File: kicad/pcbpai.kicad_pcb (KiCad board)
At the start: 2 copper layers, 91.4 x 109.2 mm, 19 parts, among them J1 Fusible, J2 Conn_01x04_Pin, J3 Input 24 V, J4 Boton Encendido, J5 Parada de Emergencia, J6 Conn_01x06_Pin, J8 Conn_01x09_Pin, M1 MountingHole_2.5mm_Pad, SW1 SW_Push_DPDT, U6 ATtiny85-20P

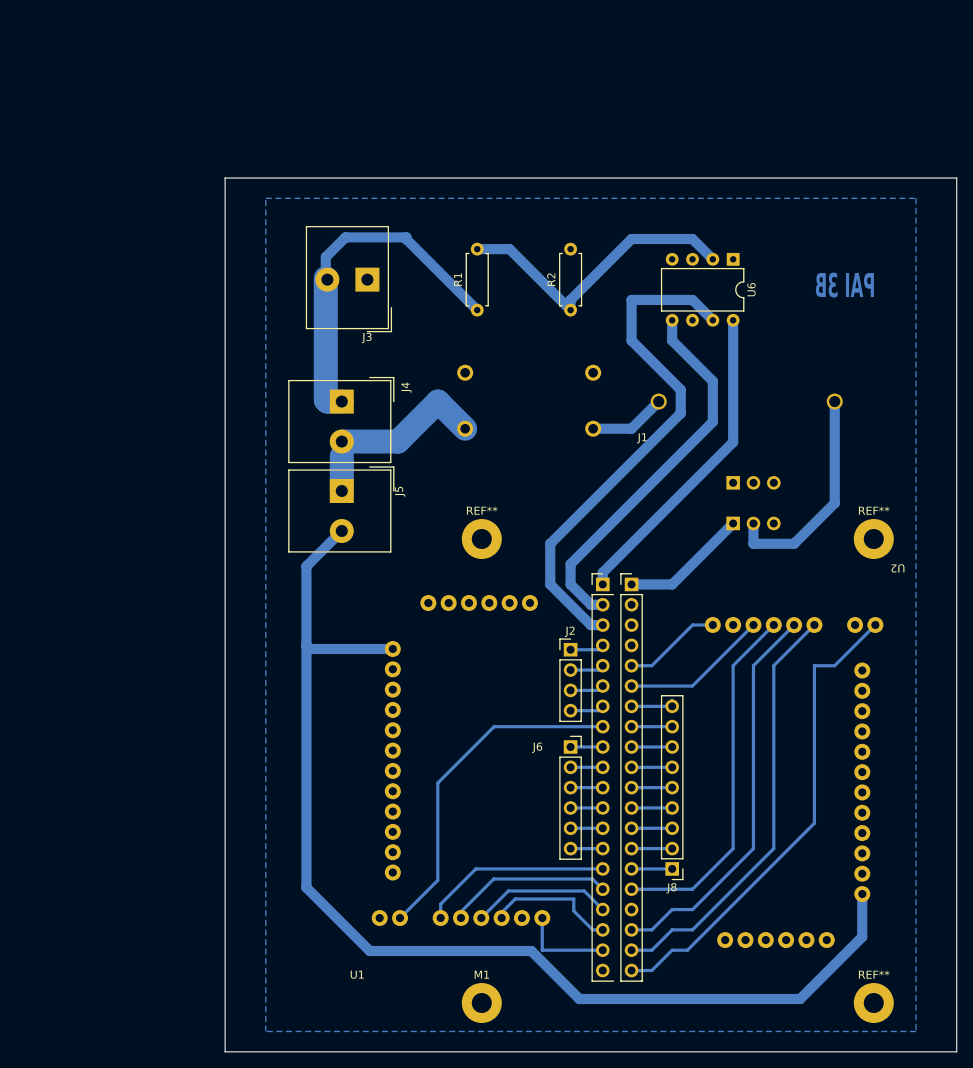
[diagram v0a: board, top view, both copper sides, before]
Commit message: add 3d models and footprints to kicad
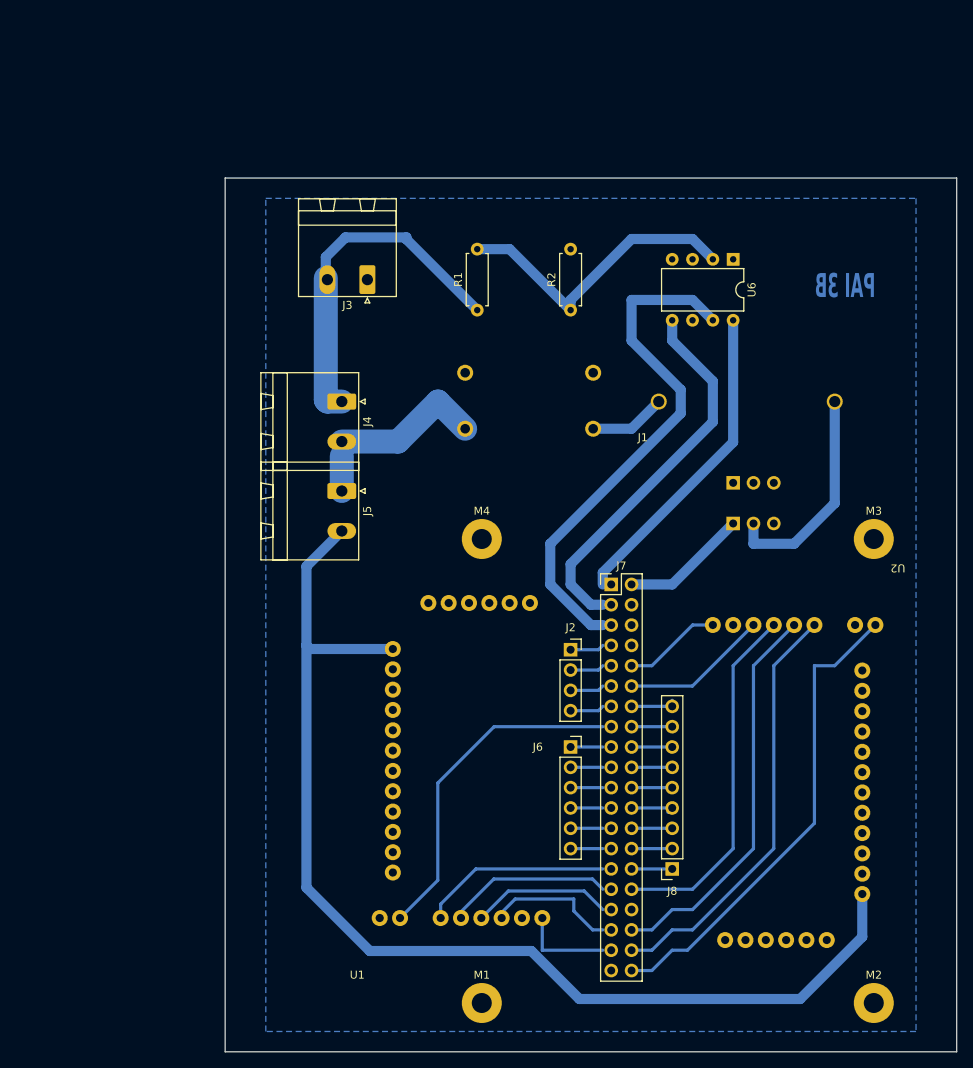
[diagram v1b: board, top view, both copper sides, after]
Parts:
- removed U3: ~, libpai:raspberry
- added J7: Raspberry GPIO, Connector_PinHeader_2.54mm:PinHeader_2x20_P2.54mm_Vertical, F.Cu at (170.2, 106.7)
- J2: footprint Connector_PinHeader_2.54mm:PinHeader_1x04_P2.54mm_Vertical -> Connector_PinSocket_2.54mm:PinSocket_1x04_P2.54mm_Vertical
- J3, J4, J5: footprint TerminalBlock_Altech:Altech_AK300_1x02_P5.00mm_45-Degree -> Connector_Phoenix_MSTB:PhoenixContact_MSTBA_2,5_2-G_1x02_P5.00mm_Horizontal
- J8: footprint Connector_PinHeader_2.54mm:PinHeader_1x09_P2.54mm_Vertical -> Connector_PinSocket_2.54mm:PinSocket_1x09_P2.54mm_Vertical
- SW1: footprint libpai:pulsador -> PAI:pulsador
- U1, U2: footprint libpai:Pololu MAX 14870 Dual Shield Arduino -> PAI:Pololu MAX 14870 Dual Shield Arduino
- renumbered REF** to M2, REF** to M3, REF** to M4

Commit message: center raspberry mounting holes
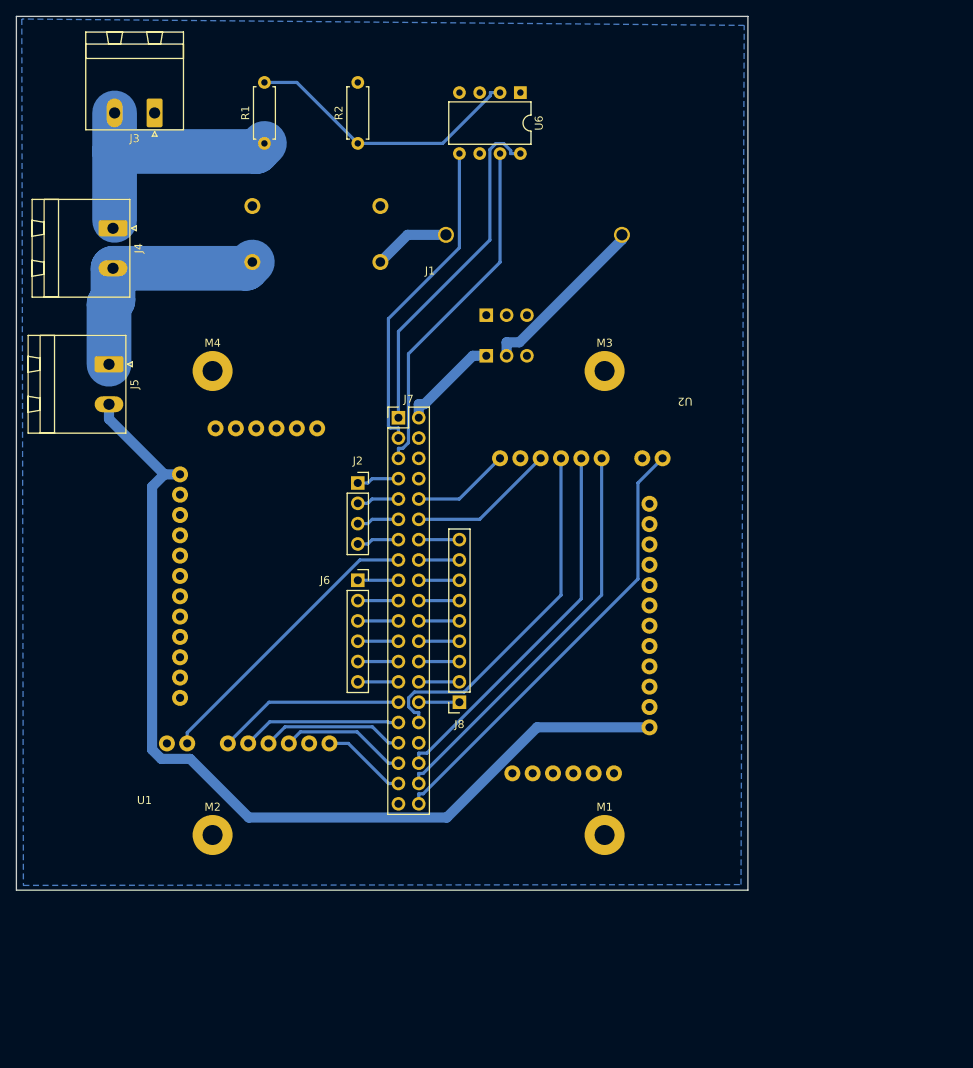
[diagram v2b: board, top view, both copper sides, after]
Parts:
- moved M2 85.3 mm to (120.3, 138.0)
- moved M3 39.7 mm to (169.3, 80.0)
- moved M4 39.7 mm to (120.3, 80.0)
- moved SW1 37.3 mm to (153.5, 76.9)
- moved J4 35.9 mm to (107.9, 62.2)
- moved U1 34.4 mm to (111.8, 134.2)
- moved J8 33.8 mm to (151.2, 121.4)
- moved U4 33.8 mm to (142.3, 67.4)
- moved R1 33.8 mm to (126.8, 51.5)
- moved J2 33.8 mm to (138.5, 94.0)
- moved J6 33.8 mm to (138.5, 106.2)
- moved J7 33.8 mm to (143.6, 85.8)
- moved R2 33.8 mm to (138.5, 51.5)
- moved U2 33.8 mm to (179.4, 83.3)
- moved U6 33.8 mm to (158.8, 45.2)
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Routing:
- net Net-(J5-Pin_2): track 141.2 -> 119.0 mm
- net Net-(J7-Pin_5): track 64.7 -> 43.7 mm
- net +24V: track 43.5 -> 33.7 mm
- net Net-(J7-Pin_3): track 47.6 -> 40.3 mm
- net Net-(J4-Pin_2): track 23.3 -> 30.0 mm
- net Net-(J7-Pin_15): track 42.4 -> 36.7 mm
- net Net-(J1-Pin_2): track 27.6 -> 22.0 mm
- net Net-(J7-Pin_40): track 59.9 -> 56.1 mm
- net Net-(J7-Pin_1): track 39.8 -> 43.1 mm
- net Net-(J7-Pin_2): track 15.9 -> 12.6 mm
- net Net-(J7-Pin_38): track 53.1 -> 50.4 mm
- net Net-(U6-XTAL1/PB3): track 38.1 -> 35.5 mm
- net Net-(J7-Pin_36): track 49.5 -> 47.1 mm
- net Net-(J2-Pin_4): track 4.24 -> 5.30 mm
- net Net-(J2-Pin_2): track 4.24 -> 5.30 mm
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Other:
- board text removed: "PAI 3B"

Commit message: update libraries and change trace width
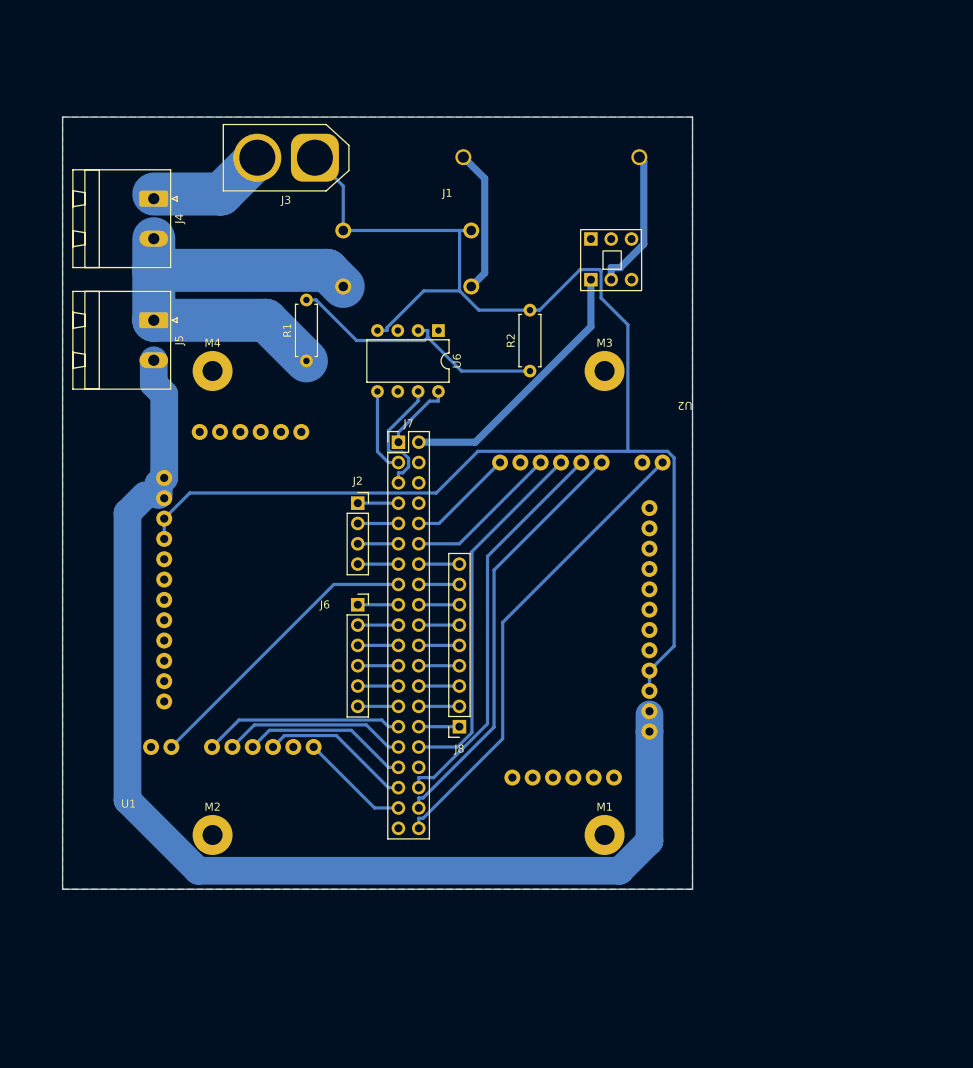
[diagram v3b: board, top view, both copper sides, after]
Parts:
- J1: footprint libpai:fusible -> PAI:fusible
- J3: footprint Connector_Phoenix_MSTB:PhoenixContact_MSTBA_2,5_2-G_1x02_P5.00mm_Horizontal -> Connector_AMASS:AMASS_XT60-M_1x02_P7.20mm_Vertical
- SW1: footprint PAI:pulsador -> PAI:switch
- U4: footprint libpai:regulador -> PAI:regulador
- moved R2 35.7 mm to (160.0, 80.0)
- moved U6 31.5 mm to (148.6, 74.9)
- moved R1 27.7 mm to (132.1, 78.7)
- moved J3 20.8 mm to (133.1, 53.3)
- moved SW1 16.2 mm to (166.6, 67.4)
- moved U4 11.8 mm to (153.7, 70.4)
- moved J1 9.95 mm to (149.7, 58.3)
- moved J5 7.85 mm to (113.0, 73.7)
- moved J4 6.30 mm to (113.0, 58.5)
- moved J6 3.06 mm to (138.5, 109.2)
- moved J7 3.06 mm to (143.6, 88.9)
- moved J8 3.06 mm to (151.2, 124.5)
- moved J2 2.52 mm to (138.5, 96.5)
- moved U1 2.03 mm to (109.8, 134.6)
- moved U2 0.53 mm to (179.4, 83.8)
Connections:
- R1 pad 1: +24V -> Net-(J4-Pin_2)
- U1 pad 10: unconnected-(U1-GND_2-Pad10) -> GND
- U1 pad 8: unconnected-(U1-Vin_2-Pad8) -> Net-(J5-Pin_2)
- U2 pad 10: unconnected-(U2-GND_2-Pad10) -> GND
- U2 pad 8: unconnected-(U2-Vin_2-Pad8) -> Net-(J5-Pin_2)
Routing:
- net GND: track 0.00 -> 191.9 mm
- net Net-(J7-Pin_1): track 43.1 -> 9.06 mm
- net Net-(J7-Pin_3): track 40.3 -> 10.7 mm
- net Net-(J7-Pin_5): track 43.7 -> 15.7 mm
- net Net-(J5-Pin_2): track 119.0 -> 146.8 mm
- net Net-(J4-Pin_2): track 30.0 -> 55.9 mm
- net Net-(J7-Pin_2): track 12.6 -> 33.4 mm
- net +24V: track 33.7 -> 14.8 mm
- net Net-(J1-Pin_1): track 9.60 -> 18.0 mm
- net Net-(J1-Pin_2): track 22.0 -> 17.9 mm
- net Net-(J7-Pin_31): track 19.9 -> 23.0 mm
- net Net-(J7-Pin_33): track 17.9 -> 21.0 mm
- net Net-(J7-Pin_37): track 10.7 -> 13.8 mm
- net Net-(J7-Pin_35): track 15.9 -> 19.0 mm
- net Net-(J7-Pin_36): track 47.1 -> 50.1 mm
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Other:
- board size 91.4 x 109.2 mm -> 78.7 x 96.5 mm

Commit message: add termninal blocks for sensors and 24+ zone
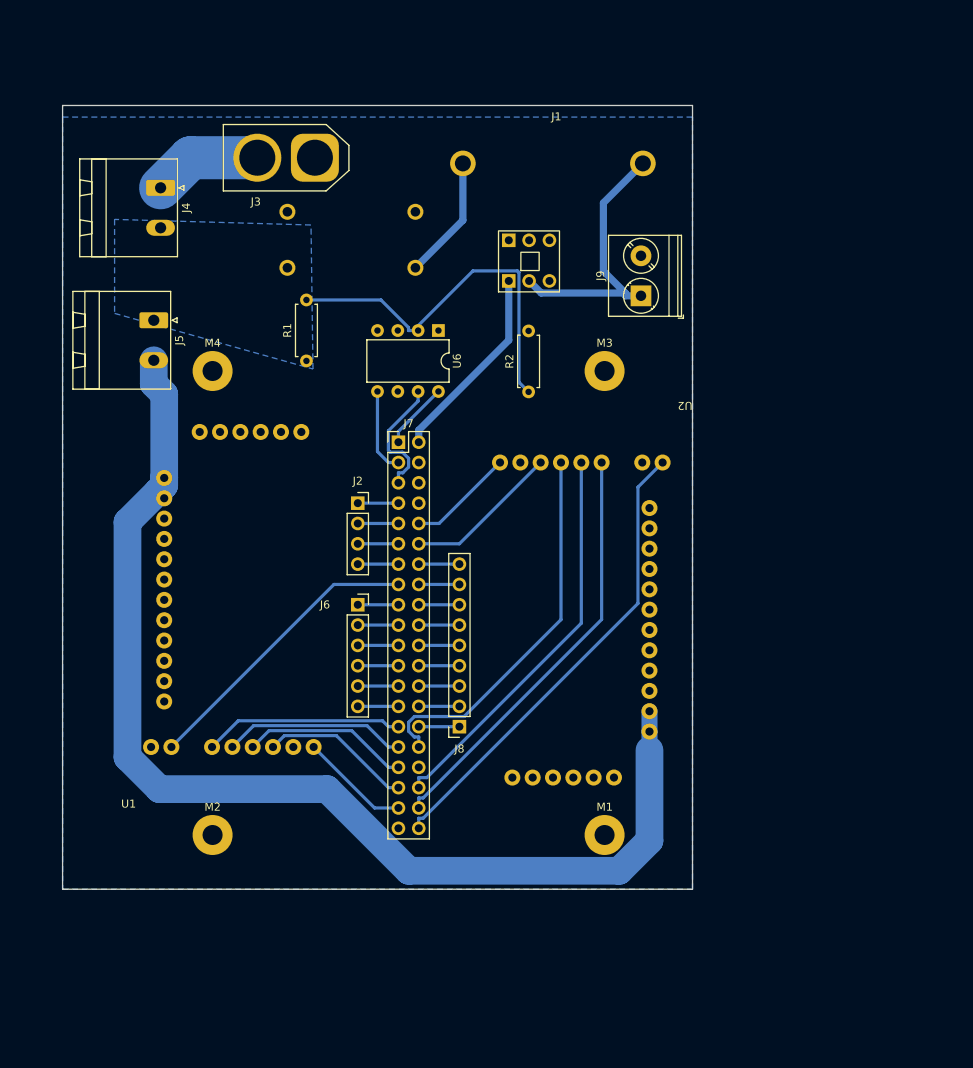
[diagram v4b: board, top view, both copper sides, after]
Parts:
- added J9: Conn_01x02_Socket, TerminalBlock_Phoenix:TerminalBlock_Phoenix_PT-1,5-2-5.0-H_1x02_P5.00mm_Horizontal, F.Cu at (173.9, 70.6)
- J1: value Fusible -> Fuse; footprint PAI:fusible -> PAI:fuse
- moved SW1 10.3 mm to (156.3, 67.6)
- moved U4 7.36 mm to (146.7, 68.1)
- moved J1 4.65 mm to (151.6, 54.0)
- moved R2 2.61 mm to (159.8, 82.6)
- moved J4 1.61 mm to (113.8, 57.1)
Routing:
- net GND: track 191.9 -> 0.00 mm
- net Net-(J4-Pin_2): track 55.9 -> 0.00 mm
- net Net-(J1-Pin_2): track 17.9 -> 34.3 mm
- net Net-(U6-XTAL1/PB3): track 34.0 -> 47.6 mm
- net Net-(J7-Pin_2): track 33.4 -> 24.8 mm
- net Net-(J5-Pin_2): track 146.8 -> 142.1 mm
- net Net-(J1-Pin_1): track 18.0 -> 15.5 mm
- net Net-(J7-Pin_32): track 45.8 -> 47.9 mm
- net +24V: track 14.8 -> 13.6 mm
- net Net-(J7-Pin_1): track 9.06 -> 8.41 mm
- added copper zone on B.Cu, net Net-(J4-Pin_2)
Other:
- board size 78.7 x 96.5 mm -> 78.7 x 98 mm

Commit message: finish pcb
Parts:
- removed SW1: SW_Push_DPDT, PAI:switch
- removed U1, U2: ~, PAI:Pololu MAX 14870 Dual Shield Arduino
- added D1: ~, Connector_PinHeader_2.54mm:PinHeader_2x04_P2.54mm_Vertical, F.Cu at (159.0, 86.9)
- added D2: ~, Connector_PinHeader_2.54mm:PinHeader_2x04_P2.54mm_Vertical, F.Cu at (159.0, 123.0)
- added D3: ~, Connector_PinHeader_2.54mm:PinHeader_2x04_P2.54mm_Vertical, F.Cu at (129.0, 94.8)
- added D4: ~, Connector_PinHeader_2.54mm:PinHeader_2x04_P2.54mm_Vertical, F.Cu at (129.0, 130.1)
- added J10: Conn_01x02_Socket, Connector_Phoenix_MSTB:PhoenixContact_MSTBA_2,5_2-G_1x02_P5.00mm_Horizontal, F.Cu at (167.2, 93.5)
- added J11: Conn_01x02_Socket, Connector_Phoenix_MSTB:PhoenixContact_MSTBA_2,5_2-G_1x02_P5.00mm_Horizontal, F.Cu at (120.8, 124.8)
- added J12: Conn_01x02_Socket, Connector_Phoenix_MSTB:PhoenixContact_MSTBA_2,5_2-G_1x02_P5.00mm_Horizontal, F.Cu at (120.8, 88.5)
- J2: value Conn_01x04_Pin -> Conn_01x08_Socket; footprint Connector_PinSocket_2.54mm:PinSocket_1x04_P2.54mm_Vertical -> Connector_PinSocket_2.54mm:PinSocket_1x08_P2.54mm_Vertical
- J6: value Conn_01x06_Pin -> Conn_01x08_Socket; footprint Connector_PinSocket_2.54mm:PinSocket_1x06_P2.54mm_Vertical -> Connector_PinSocket_2.54mm:PinSocket_1x08_P2.54mm_Vertical
- J8: value Conn_01x09_Pin -> Conn_01x02_Socket; footprint Connector_PinSocket_2.54mm:PinSocket_1x09_P2.54mm_Vertical -> Connector_Phoenix_MSTB:PhoenixContact_MSTBA_2,5_2-G_1x02_P5.00mm_Horizontal
- U4: footprint PAI:regulador -> PAI:regulator
- moved J3 37.5 mm to (170.6, 51.0)
- moved J9 28.7 mm to (154.5, 49.5), turned to 180 degrees
- moved J4 27.7 mm to (141.5, 54.8), turned to 180 degrees
- moved U4 23.3 mm to (123.5, 70.0), turned to 0 degrees
- moved R2 22.9 mm to (137.0, 81.8)
- moved J2 21.0 mm to (135.1, 117.2), turned to 180 degrees
- moved J5 20.0 mm to (119.5, 54.8), turned to 180 degrees
- moved J6 17.8 mm to (153.0, 98.9)
- moved J8 16.8 mm to (167.2, 129.5), turned to 90 degrees
- moved J1 11.2 mm to (146.5, 64.0)
- moved U6 8.78 mm to (156.8, 71.8)
- moved R1 5.00 mm to (130.0, 74.2), turned to -90 degrees
- moved J7 4.01 mm to (142.8, 85.0)
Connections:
- net Net-(J7-Pin_1) renamed +3.3V
- J5 pad 2: Net-(J5-Pin_2) -> Net-(J10-Pin_2)
- J7 pad 10: Net-(J7-Pin_10) -> unconnected-(J7-Pin_10-Pad10)
- J7 pad 11: Net-(J2-Pin_3) -> Net-(D3-EL)
- J7 pad 13: Net-(J2-Pin_4) -> Net-(D3-PWMR)
- J7 pad 14: Net-(J7-Pin_14) -> unconnected-(J7-Pin_14-Pad14)
- J7 pad 16: Net-(J7-Pin_16) -> Net-(D1-PWMR)
- J7 pad 17: Net-(J6-Pin_1) -> Net-(J2-Pin_8)
- J7 pad 18: Net-(J7-Pin_18) -> Net-(D1-PWML)
- J7 pad 19: Net-(J6-Pin_2) -> Net-(J2-Pin_7)
- J7 pad 2: Net-(J7-Pin_2) -> unconnected-(J7-Pin_2-Pad2)
- J7 pad 20: Net-(J7-Pin_20) -> Net-(J6-Pin_1)
- J7 pad 21: Net-(J6-Pin_3) -> Net-(J2-Pin_6)
- J7 pad 22: Net-(J7-Pin_22) -> Net-(J6-Pin_2)
- J7 pad 23: Net-(J6-Pin_4) -> Net-(J2-Pin_5)
- J7 pad 24: Net-(J7-Pin_24) -> Net-(J6-Pin_3)
- J7 pad 25: Net-(J6-Pin_5) -> Net-(J2-Pin_4)
- J7 pad 26: Net-(J7-Pin_26) -> Net-(J6-Pin_4)
- J7 pad 27: Net-(J6-Pin_6) -> Net-(J2-Pin_3)
- J7 pad 28: Net-(J7-Pin_28) -> Net-(J6-Pin_5)
- J7 pad 29: Net-(J7-Pin_29) -> Net-(J2-Pin_2)
- J7 pad 30: Net-(J7-Pin_30) -> Net-(J6-Pin_6)
- J7 pad 31: Net-(J7-Pin_31) -> Net-(J2-Pin_1)
- J7 pad 32: Net-(J7-Pin_32) -> Net-(J6-Pin_7)
- J7 pad 34: unconnected-(J7-Pin_34-Pad34) -> Net-(J6-Pin_8)
- J7 pad 39: unconnected-(J7-Pin_39-Pad39) -> GND
- J7 pad 7: Net-(J2-Pin_1) -> unconnected-(J7-Pin_7-Pad7)
- J7 pad 9: Net-(J2-Pin_2) -> unconnected-(J7-Pin_9-Pad9)
- J8 pad 1: Net-(J7-Pin_30) -> GND
- J8 pad 2: Net-(J7-Pin_28) -> Net-(J10-Pin_2)
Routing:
- net Net-(J5-Pin_2): track 142.1 -> 0.00 mm
- net +3.3V: track 8.41 -> 123.3 mm
- net Net-(J7-Pin_32): track 47.9 -> 0.00 mm
- net Net-(J4-Pin_2): track 0.00 -> 41.4 mm
- net Net-(D2-PWML): track 58.7 -> 17.5 mm
- net Net-(D2-PWMR): track 53.0 -> 13.6 mm
- net Net-(D2-EL): track 49.6 -> 16.2 mm
- net Net-(D3-EL): track 0.00 -> 26.3 mm
- net Net-(J7-Pin_29): track 25.0 -> 0.00 mm
- net Net-(J7-Pin_2): track 24.8 -> 0.00 mm
- net Net-(J7-Pin_31): track 23.0 -> 0.00 mm
- net Net-(D1-PWML): track 0.00 -> 21.8 mm
- net Net-(D3-PWMR): track 0.00 -> 20.0 mm
- net Net-(U6-XTAL1/PB3): track 47.6 -> 28.6 mm
- net Net-(D1-PWMR): track 0.00 -> 17.0 mm
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- added copper zone on B.Cu, net Net-(J10-Pin_2)
- removed copper zone on B.Cu, net Net-(J4-Pin_2)
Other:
- board size 78.7 x 98 mm -> 68 x 98 mm
